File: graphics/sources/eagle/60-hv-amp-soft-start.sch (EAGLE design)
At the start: 38 parts

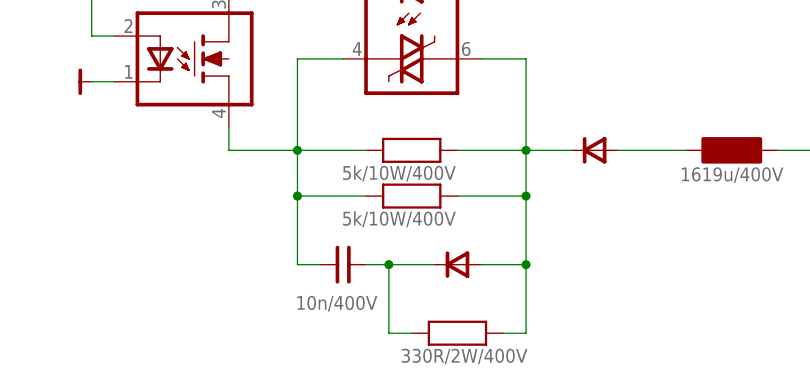
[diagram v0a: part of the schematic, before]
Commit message: Fixed some Eagle graphics and added top and bottom board views to Chapter 6
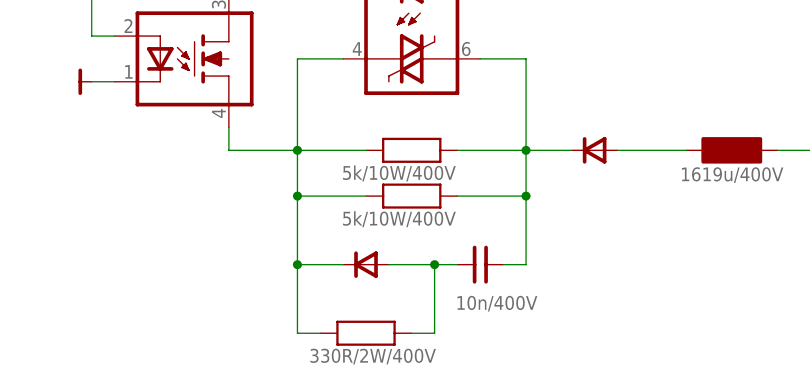
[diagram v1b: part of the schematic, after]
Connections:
- removed net N$139: C25.2, D28.C, R119.2
- new net N$1: C25.1, D28.A, R119.1
- net N$116: now also C25.2; no longer D28.A, R119.1
- net N$96: now also D28.C, R119.2; no longer C25.1
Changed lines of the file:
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@@
 <setting verticaltext="up"/>
 </settings>
-<grid distance="0.1" unitdist="inch" unit="inch" style="lines" multiple="1" display="yes" altdistance="0.025" altunitdist="inch" altunit="inch"/>
+<grid distance="0.1" unitdist="inch" unit="inch" style="lines" multiple="1" display="no" altdistance="0.025" altunitdist="inch" altunit="inch"/>
 <layers>
 <layer number="91" name="Nets" color="34" fill="1" visible="yes" active="yes"/>
@@
 <instance part="$52" gate="A" x="66.04" y="93.98"/>
 <instance part="$51" gate="A" x="60.96" y="58.42" rot="R180"/>
-<instance part="C25" gate="A" x="55.88" y="22.86" smashed="yes">
-<attribute name="VALUE" x="59.69" y="19.3675" size="1.524" layer="96" rot="R180"/>
+<instance part="C25" gate="A" x="71.12" y="22.86" smashed="yes">
+<attribute name="VALUE" x="77.47" y="19.3675" size="1.524" layer="96" rot="R180"/>
 </instance>
 <instance part="C26" gate="A" x="71.12" y="134.62" smashed="yes">
@@
 <attribute name="VALUE" x="50.6412" y="145.5738" size="1.524" layer="96" rot="MR180"/>
 </instance>
-<instance part="R119" gate="A" x="68.58" y="15.24" smashed="yes" rot="R180">
-<attribute name="VALUE" x="76.3588" y="13.4938" size="1.524" layer="96" rot="R180"/>
+<instance part="R119" gate="A" x="58.42" y="15.24" smashed="yes" rot="R180">
+<attribute name="VALUE" x="66.1988" y="13.4938" size="1.524" layer="96" rot="R180"/>
 </instance>
 <instance part="$62" gate="G$1" x="154.94" y="121.92" rot="R270"/>
@@
 <instance part="$53" gate="A" x="83.82" y="86.36" rot="R270"/>
 <instance part="$54" gate="A" x="83.82" y="71.12" rot="R270"/>
-<instance part="D28" gate="A" x="68.58" y="22.86" smashed="yes" rot="R180"/>
+<instance part="D28" gate="A" x="58.42" y="22.86" smashed="yes" rot="R180"/>
 <instance part="D27" gate="A" x="58.42" y="134.62" smashed="yes"/>
 <instance part="F1" gate="A" x="43.18" y="96.52" smashed="yes" rot="R90">
@@
 </segment>
 </net>
-<net name="N$96" class="1">
-<segment>
-<wire x1="55.88" y1="45.72" x2="50.8" y2="45.72" width="0.1524" layer="91"/>
-<wire x1="58.42" y1="35.56" x2="50.8" y2="35.56" width="0.1524" layer="91"/>
-<wire x1="50.8" y1="35.56" x2="50.8" y2="30.48" width="0.1524" layer="91"/>
-<wire x1="50.8" y1="30.48" x2="58.42" y2="30.48" width="0.1524" layer="91"/>
-<wire x1="50.8" y1="45.72" x2="50.8" y2="35.56" width="0.1524" layer="91"/>
-<wire x1="50.8" y1="30.48" x2="50.8" y2="22.86" width="0.1524" layer="91"/>
-<wire x1="50.8" y1="22.86" x2="53.34" y2="22.86" width="0.1524" layer="91"/>
-<junction x="50.8" y="35.56"/>
-<junction x="50.8" y="30.48"/>
-<pinref part="N28" gate="A" pin="MT1"/>
-<pinref part="R117" gate="A" pin="2"/>
-<pinref part="R118" gate="A" pin="1"/>
-<pinref part="C25" gate="A" pin="1"/>
-<pinref part="N26" gate="A" pin="OUT2"/>
-<wire x1="43.18" y1="38.1" x2="43.18" y2="35.56" width="0.1524" layer="91"/>
-<wire x1="43.18" y1="35.56" x2="50.8" y2="35.56" width="0.1524" layer="91"/>
-</segment>
-</net>
 <net name="N$97" class="0">
 <segment>
@@
 <net name="N$116" class="1">
 <segment>
-<wire x1="73.66" y1="15.24" x2="76.2" y2="15.24" width="0.1524" layer="91"/>
 <wire x1="71.12" y1="45.72" x2="76.2" y2="45.72" width="0.1524" layer="91"/>
 <wire x1="68.58" y1="35.56" x2="76.2" y2="35.56" width="0.1524" layer="91"/>
@@
 <wire x1="76.2" y1="30.48" x2="68.58" y2="30.48" width="0.1524" layer="91"/>
 <wire x1="76.2" y1="45.72" x2="76.2" y2="35.56" width="0.1524" layer="91"/>
-<wire x1="76.2" y1="15.24" x2="76.2" y2="22.86" width="0.1524" layer="91"/>
-<wire x1="76.2" y1="22.86" x2="76.2" y2="30.48" width="0.1524" layer="91"/>
-<wire x1="71.12" y1="22.86" x2="76.2" y2="22.86" width="0.1524" layer="91"/>
 <junction x="76.2" y="35.56"/>
-<junction x="76.2" y="30.48"/>
-<junction x="76.2" y="22.86"/>
-<pinref part="R119" gate="A" pin="1"/>
 <pinref part="N28" gate="A" pin="MT2"/>
 <pinref part="R117" gate="A" pin="1"/>
 <pinref part="R118" gate="A" pin="2"/>
 <pinref part="D30" gate="A" pin="C"/>
-<pinref part="D28" gate="A" pin="A"/>
+<pinref part="C25" gate="A" pin="2"/>
+<wire x1="73.66" y1="22.86" x2="76.2" y2="22.86" width="0.1524" layer="91"/>
+<wire x1="76.2" y1="22.86" x2="76.2" y2="30.48" width="0.1524" layer="91"/>
+<junction x="76.2" y="30.48"/>
 </segment>
 </net>
@@
 <pinref part="C26" gate="A" pin="1"/>
 <pinref part="D27" gate="A" pin="C"/>
-</segment>
-</net>
-<net name="N$139" class="1">
-<segment>
-<wire x1="63.5" y1="15.24" x2="60.96" y2="15.24" width="0.1524" layer="91"/>
-<wire x1="58.42" y1="22.86" x2="60.96" y2="22.86" width="0.1524" layer="91"/>
-<wire x1="60.96" y1="22.86" x2="66.04" y2="22.86" width="0.1524" layer="91"/>
-<wire x1="60.96" y1="15.24" x2="60.96" y2="22.86" width="0.1524" layer="91"/>
-<junction x="60.96" y="22.86"/>
-<pinref part="R119" gate="A" pin="2"/>
-<pinref part="C25" gate="A" pin="2"/>
-<pinref part="D28" gate="A" pin="C"/>
 </segment>
 </net>
@@
 </segment>
 </net>
+<net name="N$96" class="1">
+<segment>
+<wire x1="53.34" y1="15.24" x2="50.8" y2="15.24" width="0.1524" layer="91"/>
+<wire x1="50.8" y1="22.86" x2="55.88" y2="22.86" width="0.1524" layer="91"/>
+<wire x1="50.8" y1="15.24" x2="50.8" y2="22.86" width="0.1524" layer="91"/>
+<pinref part="R119" gate="A" pin="2"/>
+<pinref part="D28" gate="A" pin="C"/>
+<wire x1="55.88" y1="45.72" x2="50.8" y2="45.72" width="0.1524" layer="91"/>
+<wire x1="58.42" y1="35.56" x2="50.8" y2="35.56" width="0.1524" layer="91"/>
+<wire x1="50.8" y1="35.56" x2="50.8" y2="30.48" width="0.1524" layer="91"/>
+<wire x1="50.8" y1="30.48" x2="58.42" y2="30.48" width="0.1524" layer="91"/>
+<wire x1="50.8" y1="45.72" x2="50.8" y2="35.56" width="0.1524" layer="91"/>
+<junction x="50.8" y="35.56"/>
+<pinref part="N28" gate="A" pin="MT1"/>
+<pinref part="R117" gate="A" pin="2"/>
+<pinref part="R118" gate="A" pin="1"/>
+<pinref part="N26" gate="A" pin="OUT2"/>
+<wire x1="43.18" y1="38.1" x2="43.18" y2="35.56" width="0.1524" layer="91"/>
+<wire x1="43.18" y1="35.56" x2="50.8" y2="35.56" width="0.1524" layer="91"/>
+<wire x1="50.8" y1="22.86" x2="50.8" y2="30.48" width="0.1524" layer="91"/>
+<junction x="50.8" y="22.86"/>
+<junction x="50.8" y="30.48"/>
+</segment>
+</net>
+<net name="N$1" class="1">
+<segment>
+<pinref part="D28" gate="A" pin="A"/>
+<wire x1="60.96" y1="22.86" x2="66.04" y2="22.86" width="0.1524" layer="91"/>
+<wire x1="66.04" y1="15.24" x2="66.04" y2="22.86" width="0.1524" layer="91"/>
+<wire x1="63.5" y1="15.24" x2="66.04" y2="15.24" width="0.1524" layer="91"/>
+<pinref part="R119" gate="A" pin="1"/>
+<pinref part="C25" gate="A" pin="1"/>
+<wire x1="66.04" y1="22.86" x2="68.58" y2="22.86" width="0.1524" layer="91"/>
+<junction x="66.04" y="22.86"/>
+</segment>
+</net>

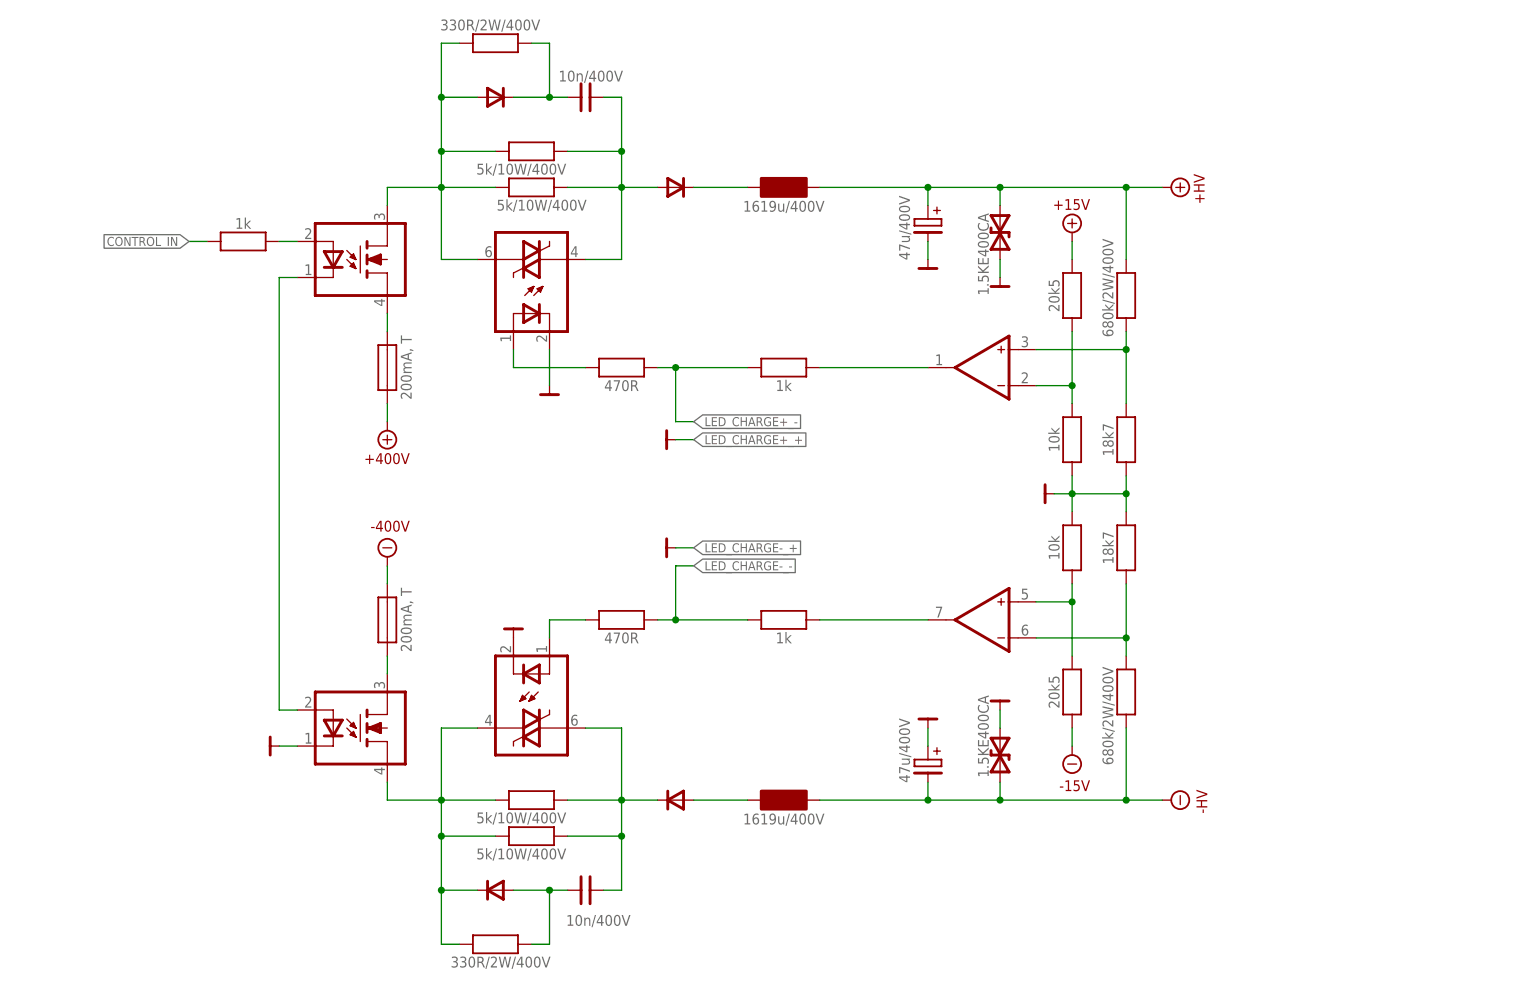
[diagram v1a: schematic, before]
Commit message: Added annotations to Eagle diagrams. Still needs textual updates.
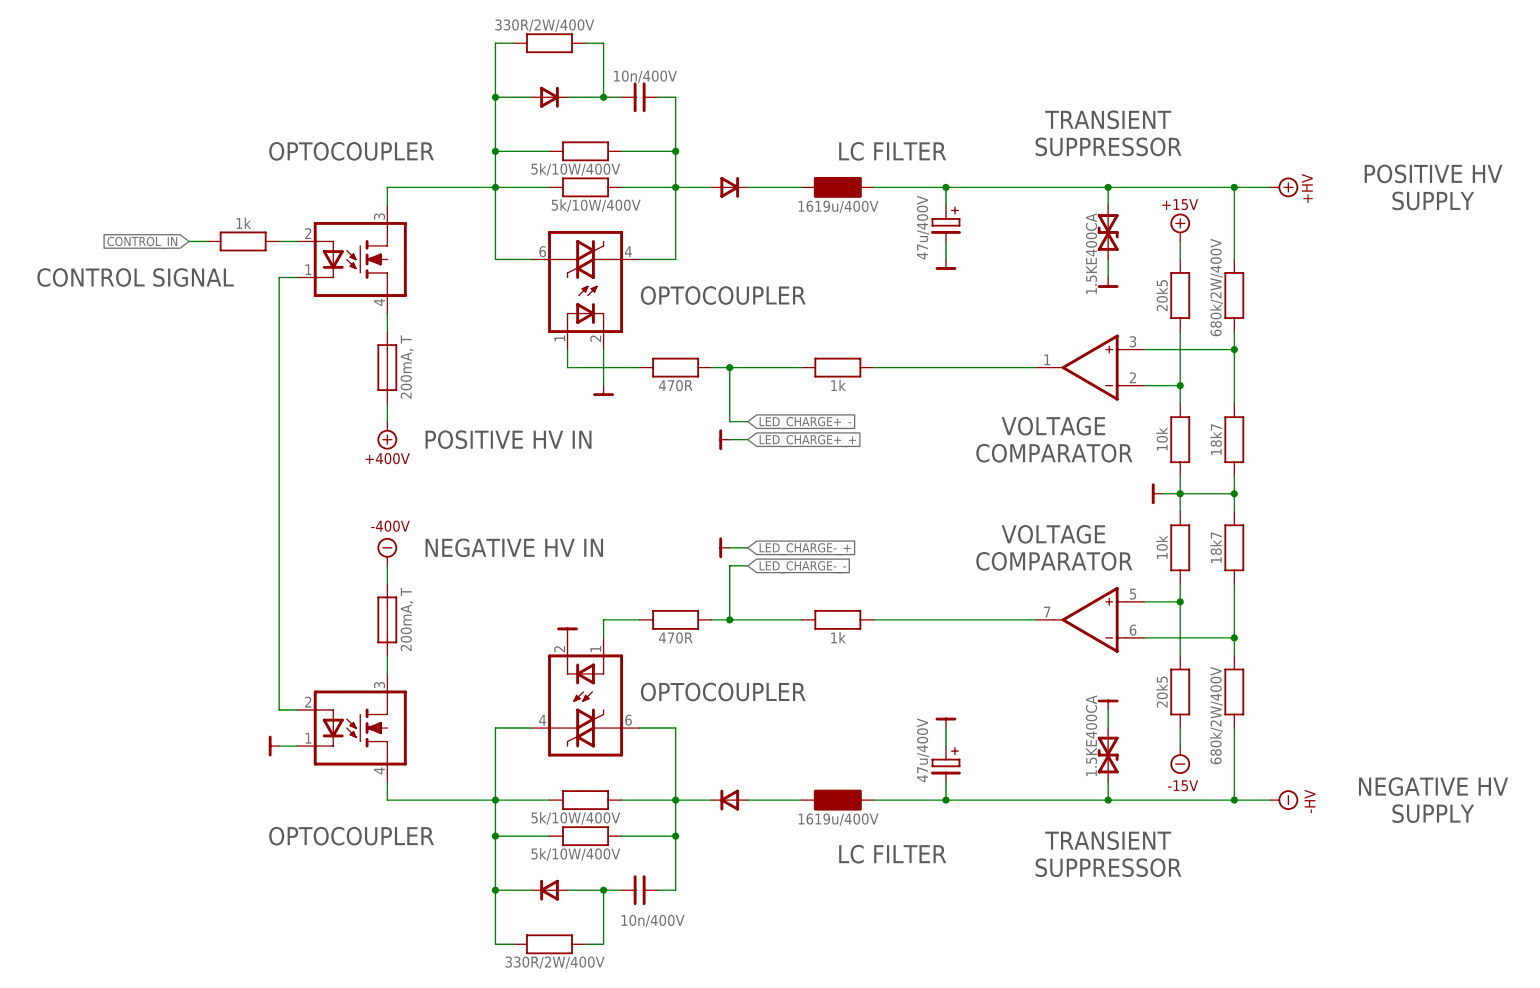
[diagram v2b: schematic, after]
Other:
- note added: "CONTROL SIGNAL"
- note added: "LC FILTER"
- note added: "NEGATIVE HV IN"
- note added: "NEGATIVE HV SUPPLY"
- note added: "OPTOCOUPLER"
- note added: "POSITIVE HV IN"
- note added: "POSITIVE HV SUPPLY"
- note added: "TRANSIENT SUPPRESSOR"
- note added: "VOLTAGE COMPARATOR"
